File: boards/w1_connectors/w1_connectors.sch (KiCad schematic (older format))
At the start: 22 parts, among them J1 Conn_01x10_Female, J2 Conn_01x10_Female, J3 LevelConverterLV, J4 LevelConverterHV, J5 LevelConverterHV, J6 LevelConverterHV

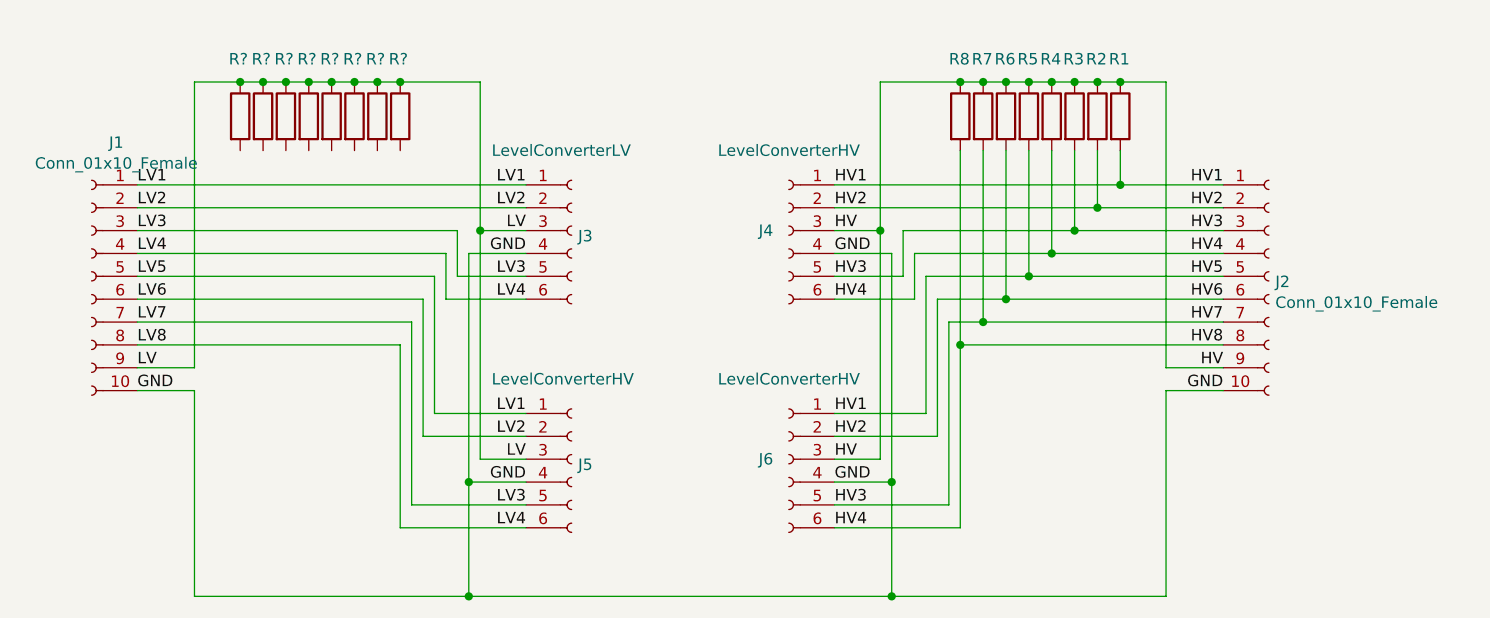
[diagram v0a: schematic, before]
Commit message: Schaltung Level Shifter fuer 8 one Wire Busleitungen
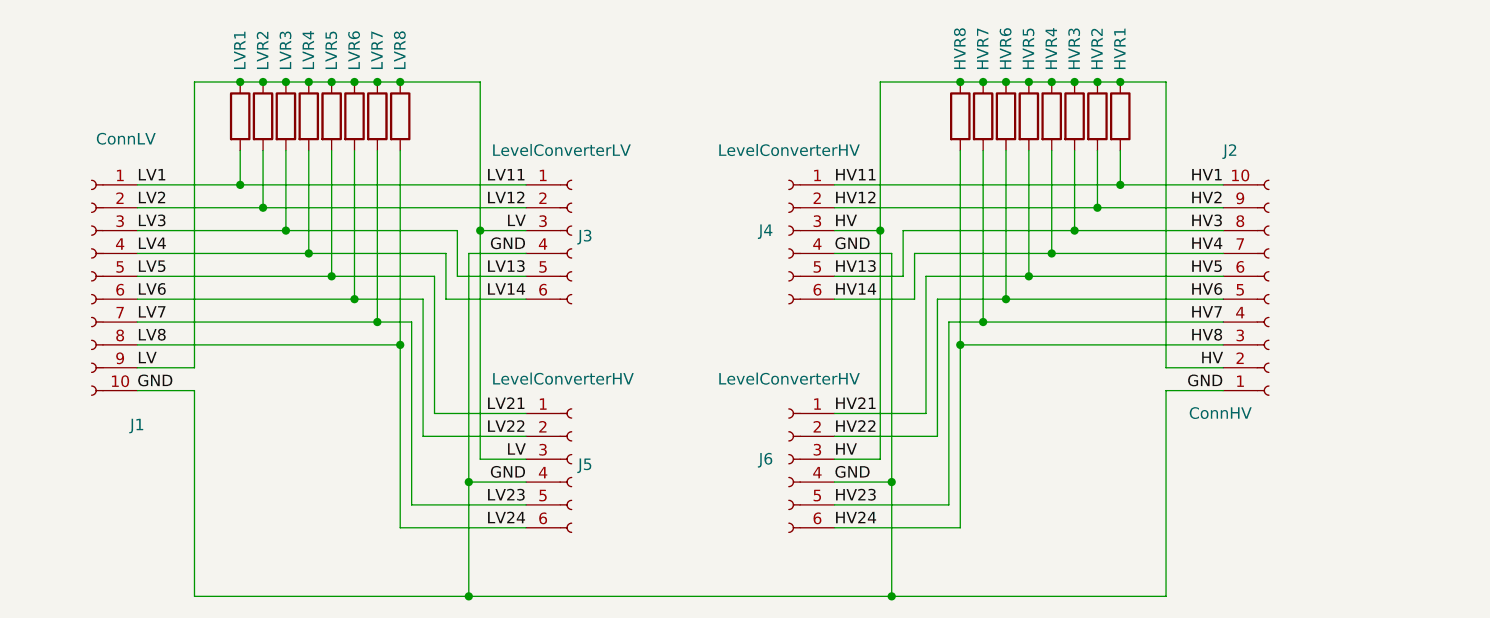
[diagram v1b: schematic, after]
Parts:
- HVR1: renamed from R1; footprint (none) -> Resistor_SMD:R_1206_3216Metric_Pad1.30x1.75mm_HandSolder
- HVR2: renamed from R2; footprint (none) -> Resistor_SMD:R_1206_3216Metric_Pad1.30x1.75mm_HandSolder
- HVR3: renamed from R3; footprint (none) -> Resistor_SMD:R_1206_3216Metric_Pad1.30x1.75mm_HandSolder
- HVR4: renamed from R4; footprint (none) -> Resistor_SMD:R_1206_3216Metric_Pad1.30x1.75mm_HandSolder
- HVR5: renamed from R5; footprint (none) -> Resistor_SMD:R_1206_3216Metric_Pad1.30x1.75mm_HandSolder
- HVR6: renamed from R6; footprint (none) -> Resistor_SMD:R_1206_3216Metric_Pad1.30x1.75mm_HandSolder
- HVR7: renamed from R7; footprint (none) -> Resistor_SMD:R_1206_3216Metric_Pad1.30x1.75mm_HandSolder
- HVR8: renamed from R8; footprint (none) -> Resistor_SMD:R_1206_3216Metric_Pad1.30x1.75mm_HandSolder
- J1: value Conn_01x10_Female -> ConnLV; footprint (none) -> TerminalBlock_Phoenix:TerminalBlock_Phoenix_MPT-0,5-10-2.54_1x10_P2.54mm_Horizontal
- J2: value Conn_01x10_Female -> ConnHV; footprint (none) -> TerminalBlock_Phoenix:TerminalBlock_Phoenix_MPT-0,5-10-2.54_1x10_P2.54mm_Horizontal
- J3, J4, J5, J6: footprint (none) -> Connector_PinSocket_2.54mm:PinSocket_1x06_P2.54mm_Vertical
- LVR1, LVR2, LVR3, LVR4, LVR5, LVR6, LVR7, LVR8: renamed from R?; footprint (none) -> Resistor_SMD:R_1206_3216Metric_Pad1.30x1.75mm_HandSolder
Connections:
- net GND: now also J2.1 (Pin_1); no longer J2.10 (Pin_10)
- net HV: now also J2.2 (Pin_2); no longer J2.9 (Pin_9)
- net HV1: now also J2.10 (Pin_10); no longer HVR5.2, J2.1 (Pin_1), J2.5 (Pin_5), J6.1 (Pin_1)
- net LV1: now also LVR1.2; no longer J1.5 (Pin_5), J5.1 (Pin_1)
- net LV12: now reaches LVR2.2
- net LV12: now also J1.2 (Pin_2), J3.2 (Pin_2)
- net LV13: now reaches LVR3.2
- net LV13: now also J1.3 (Pin_3), J3.5 (Pin_5)
- net LV14: now reaches LVR4.2
- net LV14: now also J1.4 (Pin_4), J3.6 (Pin_6)
- net LV21: now reaches LVR5.2
- net LV21: now also J1.5 (Pin_5), J5.1 (Pin_1)
- net LV22: now reaches LVR6.2
- net LV22: now also J1.6 (Pin_6), J5.2 (Pin_2)
- net LV23: now reaches LVR7.2
- net LV23: now also J1.7 (Pin_7), J5.5 (Pin_5)
- net LV24: now reaches LVR8.2
- net LV24: now also J1.8 (Pin_8), J5.6 (Pin_6)
- removed net HV2: HVR2.2, HVR6.2, J2.2 (Pin_2), J2.6 (Pin_6), J4.2 (Pin_2), J6.2 (Pin_2)
- removed net HV3: HVR3.2, HVR7.2, J2.3 (Pin_3), J2.7 (Pin_7), J4.5 (Pin_5), J6.5 (Pin_5)
- removed net HV4: HVR4.2, HVR8.2, J2.4 (Pin_4), J2.8 (Pin_8), J4.6 (Pin_6), J6.6 (Pin_6)
- removed net LV2: J1.2 (Pin_2), J1.6 (Pin_6), J3.2 (Pin_2), J5.2 (Pin_2)
- removed net LV3: J1.3 (Pin_3), J1.7 (Pin_7), J3.5 (Pin_5), J5.5 (Pin_5)
- removed net LV4: J1.4 (Pin_4), J1.8 (Pin_8), J3.6 (Pin_6), J5.6 (Pin_6)
- new net HV12: HVR2.2, J2.9 (Pin_9), J4.2 (Pin_2)
- new net HV13: HVR3.2, J2.8 (Pin_8), J4.5 (Pin_5)
- new net HV14: HVR4.2, J2.7 (Pin_7), J4.6 (Pin_6)
- new net HV21: HVR5.2, J2.6 (Pin_6), J6.1 (Pin_1)
- new net HV22: HVR6.2, J2.5 (Pin_5), J6.2 (Pin_2)
- new net HV23: HVR7.2, J2.4 (Pin_4), J6.5 (Pin_5)
- new net HV24: HVR8.2, J2.3 (Pin_3), J6.6 (Pin_6)
